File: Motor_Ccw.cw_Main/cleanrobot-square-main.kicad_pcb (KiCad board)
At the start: 2 copper layers, 77.9 x 39.9 mm, 67 parts, among them J1 KF128-3.81-3P, J2 KF128-3.81-2P, J3 Conn_01x04, J5 KF128-3.81-2P, J8 Conn_01x04, SW1 6x6x5mm, SW2 6x6x5mm, U1 STM32F030C8T6, U13 LMV358TP-SR, U2 XL1509-5.0E1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

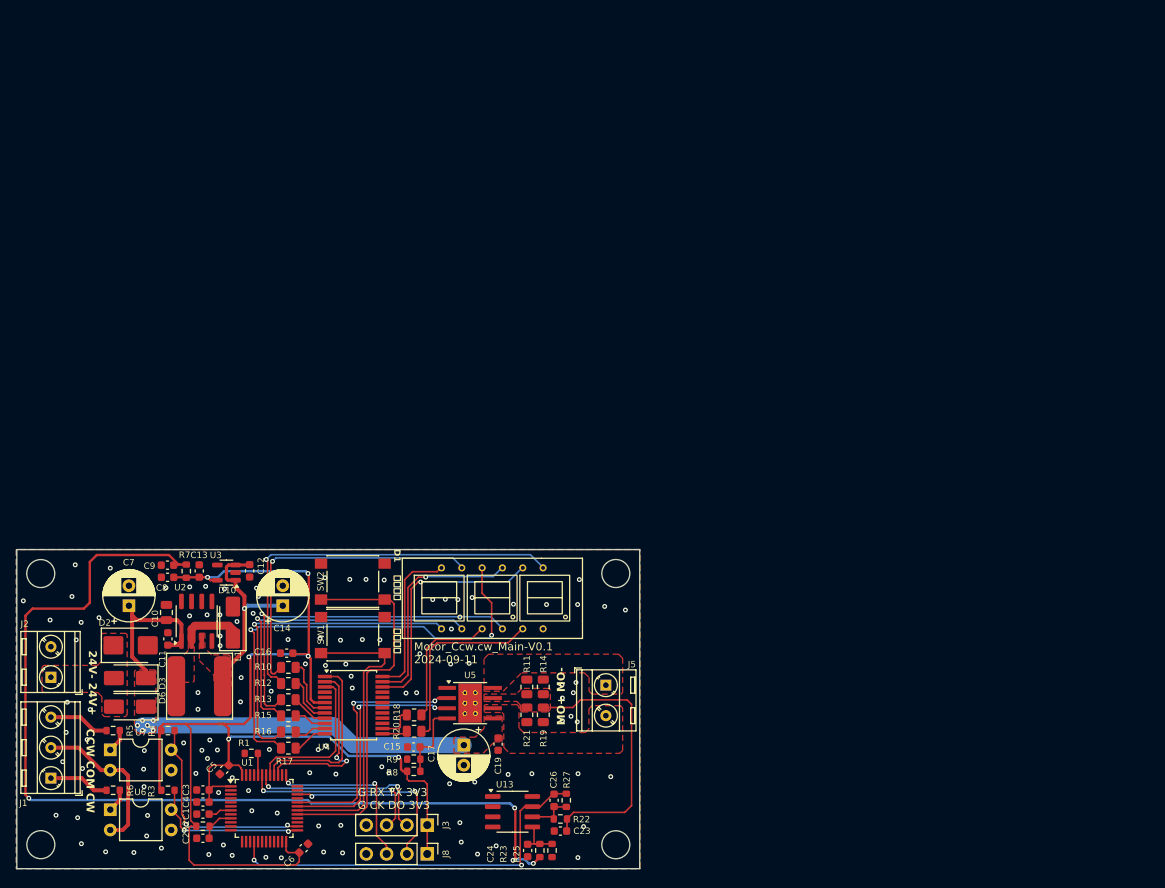
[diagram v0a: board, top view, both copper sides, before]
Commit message: 修改封装，修改原理图
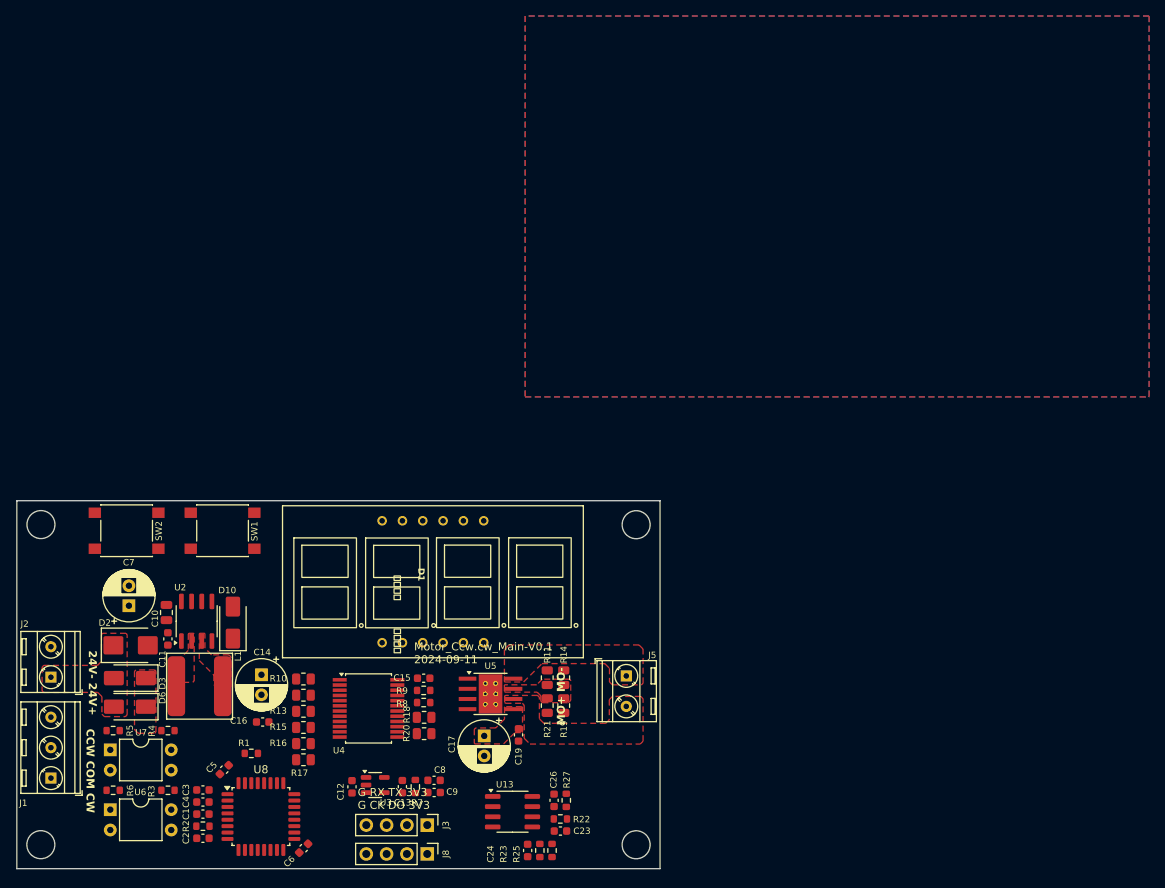
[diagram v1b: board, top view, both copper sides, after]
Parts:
- removed U1: STM32F030C8T6, Package_QFP:LQFP-48_7x7mm_P0.5mm
- added U8: STM32F030K6Tx, Package_QFP:LQFP-32_7x7mm_P0.8mm, F.Cu at (146.5, 110.4)
- moved C9 43.8 mm to (168.2, 107.4), turned to 0 degrees
- moved C8 41.9 mm to (168.2, 105.8), turned to 0 degrees
- moved R7 39.3 mm to (165.8, 106.6), turned to -90 degrees
- moved C13 37.0 mm to (164.2, 106.6), turned to -90 degrees
- moved U3 32.4 mm to (160.8, 106.4), turned to 0 degrees
- moved C12 29.9 mm to (157.9, 106.7), turned to 90 degrees
- moved SW2 29.0 mm to (129.7, 74.6), turned to 0 degrees
- moved SW1 20.9 mm to (141.7, 74.6), turned to 0 degrees
- moved C16 9.11 mm to (146.8, 98.5)
- moved C14 9.03 mm to (146.6, 92.6), turned to -90 degrees
- moved C15 8.68 mm to (166.9, 93.1)
- moved R8 8.68 mm to (166.9, 96.1)
- moved R9 8.68 mm to (166.9, 94.6)
- moved D1 3.82 mm to (167.2, 80.4)
- moved C17 2.80 mm to (174.4, 100.3)
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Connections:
- U4 pad 21: unconnected-(U4-GR3-Pad21) -> /main/COM3
- U4 pad 22: /main/COM3 -> GND
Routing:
- net +3V3: track 166.5 -> 0.00 mm, vias 6 -> 0
- net +3.3VA: track 122.2 -> 0.00 mm, vias 4 -> 0
- net VDD: track 61.8 -> 0.00 mm, vias 6 -> 0
- net /main/F: track 57.6 -> 0.00 mm, vias 2 -> 0
- net /main/B: track 52.2 -> 0.00 mm, vias 1 -> 0
- net /main/ADC2_MOTOR: track 49.5 -> 0.00 mm, vias 2 -> 0
- net /main/SW_PWM+: track 46.6 -> 0.00 mm
- net /main/C: track 44.7 -> 0.00 mm, vias 1 -> 0
- net /main/E: track 41.0 -> 0.00 mm, vias 1 -> 0
- net /main/D: track 40.2 -> 0.00 mm, vias 1 -> 0
- net /main/A: track 40.1 -> 0.00 mm, vias 1 -> 0
- net /main/SW_PWM-: track 37.5 -> 0.00 mm
- net Net-(U5-ISEN): track 34.6 -> 0.00 mm
- net /main/PWM_RIGHT2: track 31.6 -> 0.00 mm, vias 2 -> 0
- net /main/PWM_RIGHT1: track 31.1 -> 0.00 mm, vias 2 -> 0
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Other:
- board size 77.9 x 39.9 mm -> 80.4 x 46 mm
